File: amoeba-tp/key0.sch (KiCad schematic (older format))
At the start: 4 parts

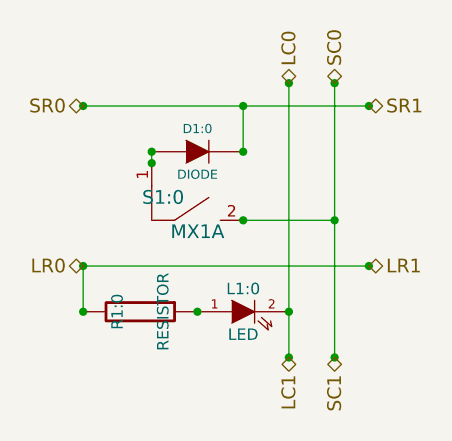
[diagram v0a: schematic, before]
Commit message: Added fill zones.
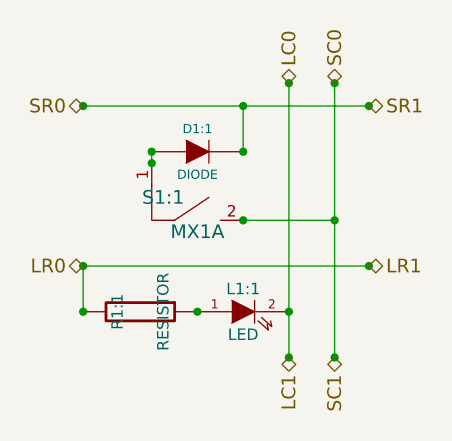
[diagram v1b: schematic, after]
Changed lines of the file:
@@
 AR Path="/55D8859F/55D7BDA8" Ref="S1:1"  Part="1"
 AR Path="/55D89165/55D7BDA8" Ref="S2:1"  Part="1"
-F 0 "S1:0" H 5450 4150 60  0000 C CNN
+F 0 "S1:1" H 5450 4150 60  0000 C CNN
 F 1 "MX1A" H 5600 4000 60  0000 C CNN
 F 2 "~" H 5600 3900 60  0000 C CNN
@@
 AR Path="/55D8859F/55D7BDAE" Ref="D1:1"  Part="1"
 AR Path="/55D89165/55D7BDAE" Ref="D2:1"  Part="1"
-F 0 "D1:0" H 5600 3550 40  0000 C CNN
+F 0 "D1:1" H 5600 3550 40  0000 C CNN
 F 1 "DIODE" H 5600 3350 40  0000 C CNN
 F 2 "~" H 5600 3450 60  0000 C CNN
@@
 AR Path="/55D8859F/55D7BDE4" Ref="L1:1"  Part="1"
 AR Path="/55D89165/55D7BDE4" Ref="L2:1"  Part="1"
-F 0 "L1:0" H 5800 4250 50  0000 C CNN
+F 0 "L1:1" H 5800 4250 50  0000 C CNN
 F 1 "LED" H 5800 4050 50  0000 C CNN
 F 2 "~" H 5800 4150 60  0000 C CNN
@@
 AR Path="/55D8859F/55D7BDEA" Ref="R1:1"  Part="1"
 AR Path="/55D89165/55D7BDEA" Ref="R2:1"  Part="1"
-F 0 "R1:0" H 5350 4050 50  0000 C CNN
+F 0 "R1:1" H 5350 4050 50  0000 C CNN
 F 1 "RESISTOR" H 5350 4250 50  0000 C CNN
 F 2 "~" H 5350 4150 60  0000 C CNN
